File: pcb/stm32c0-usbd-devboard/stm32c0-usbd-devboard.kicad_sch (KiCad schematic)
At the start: 25 parts, among them J1 USB_B_Mini, J2 PIN H 5P, J3 LEFT, J4 RIGHT, U1 USBLC6-2SC6, U2 MCP1700-3302E, U3 STM32C071K8T6, Y1 8MHz

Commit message: pcb: c0: fix crystal frequency
no physical layer changes, no revision bump.
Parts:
- Y1: value 8MHz -> 48MHz
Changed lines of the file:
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@@
 			)
 		)
-		(property "Value" "8MHz"
+		(property "Value" "48MHz"
 			(at 161.29 132.0799 90)
 			(effects

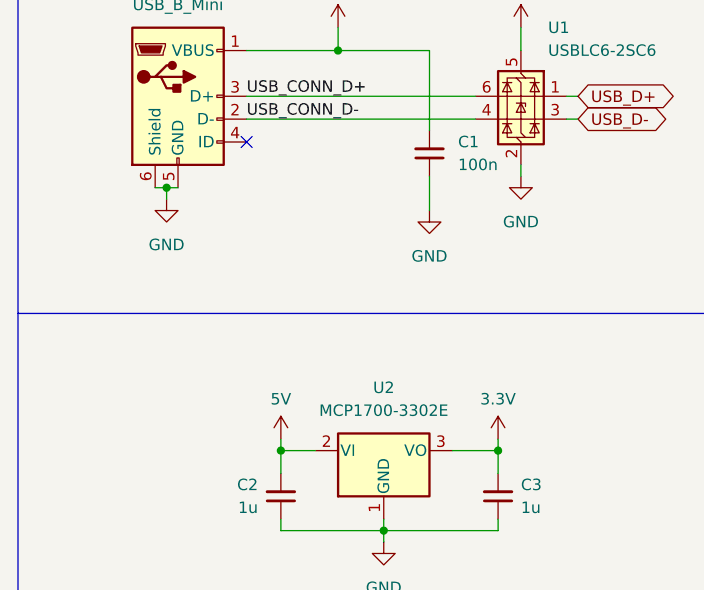
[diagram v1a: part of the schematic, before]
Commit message: pcb: c0: upgrade to kicad 10
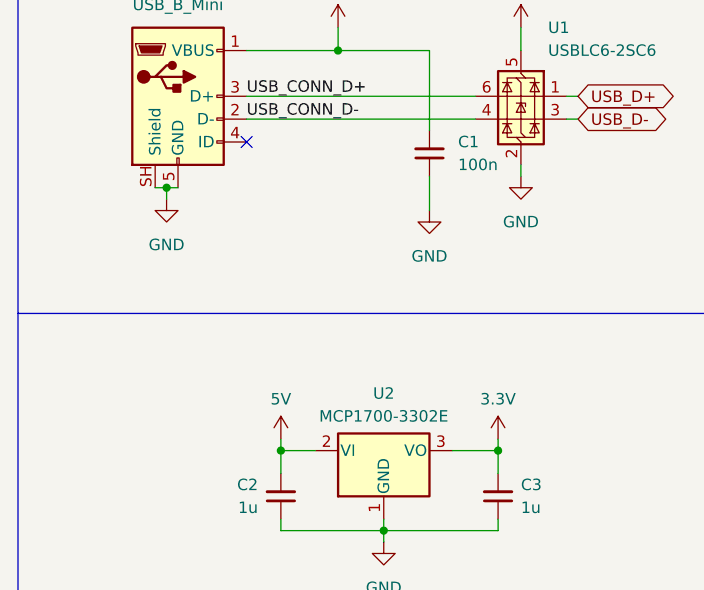
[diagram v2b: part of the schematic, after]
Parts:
- U2: symbol Regulator_Linear:MCP1700x-330xxTO -> custom:MCP1700x-330xxTO
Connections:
- net GND: now also J1.SH (Shield); no longer J1.6 (Shield)
